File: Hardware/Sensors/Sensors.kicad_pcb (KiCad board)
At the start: 2 copper layers, 24 x 24 mm, 5 parts, among them J1 Conn_01x02, SW1 SW_Reed, SW2 SW_Reed

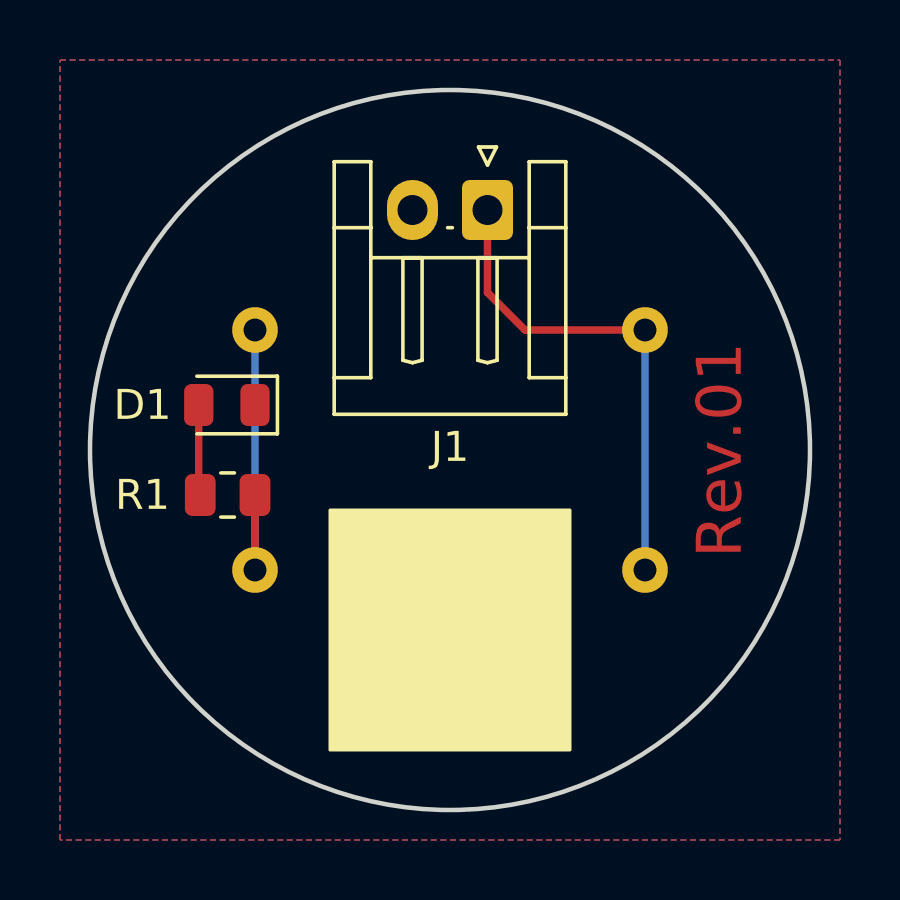
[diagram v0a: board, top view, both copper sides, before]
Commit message: New PCB.
- Added hall effect sensor.
- Increased distance for reed switch mount holes.
- Cables for connections will be soldered on pads instead of PTH.
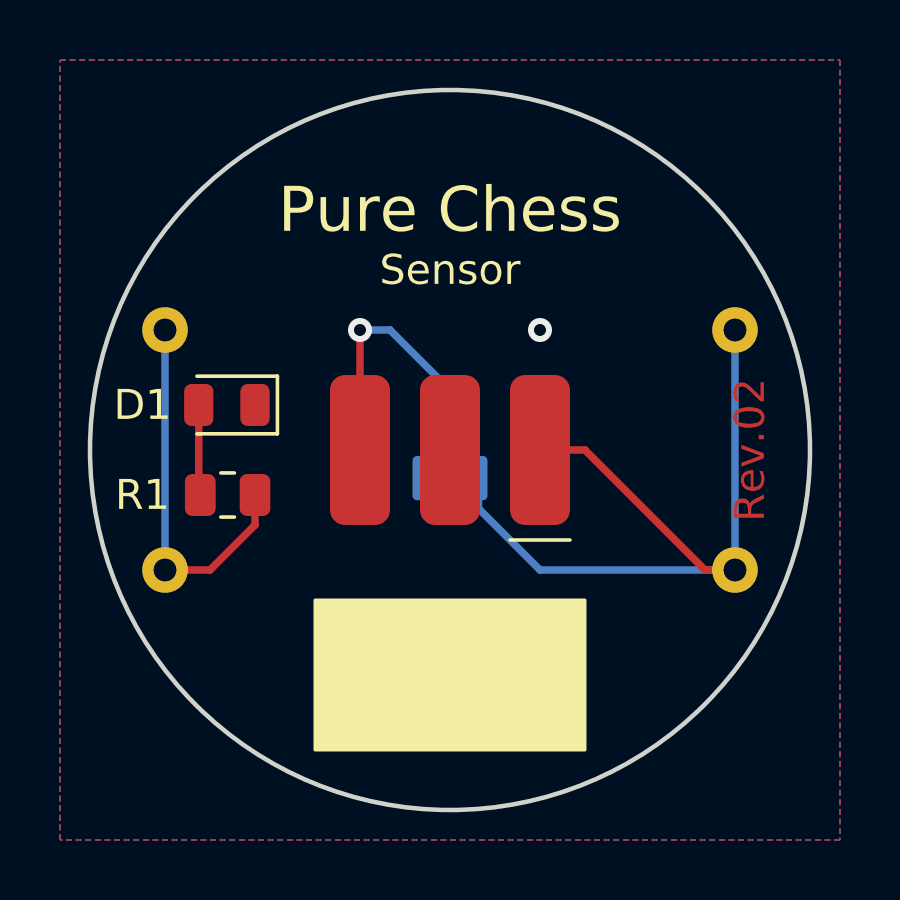
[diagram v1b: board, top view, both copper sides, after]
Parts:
- added U1: A1369xUA-24, Package_TO_SOT_SMD:SOT-23, B.Cu at (80.0, 50.0)
- J1: value Conn_01x02 -> Conn_01x03; footprint Connector_JST:JST_EH_S2B-EH_1x02_P2.50mm_Horizontal -> TOMA_Systems:Pad_03x01
- moved J1 8.10 mm to (80.0, 50.0)
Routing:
- net Net-(SW1-Pad1): track 16.5 -> 26.6 mm
- net Net-(J1-Pad3): track 0.00 -> 8.89 mm, vias 0 -> 1
- net Net-(R1-Pad1): track 10.5 -> 12.6 mm
- net Net-(D1-Pad1): vias 0 -> 1
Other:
- net class Default removed
- board text added: "Pure Chess"
- board text added: "Rev.02"
- board text added: "Sensor"
- board text removed: "Rev.01"
